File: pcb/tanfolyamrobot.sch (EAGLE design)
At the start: 85 parts, among them IC1 STM32F10XRXT6, IC2 7805, IC4 FT232RL, IC5 LD117AS33TR, M1 DRV8833, Q1 AO4407A, Q2 BSS123, Q3 BSS123, Q4 BSS123, X1 CSTCE08M, X2 PWR, X6 KUSBVX-BS1N

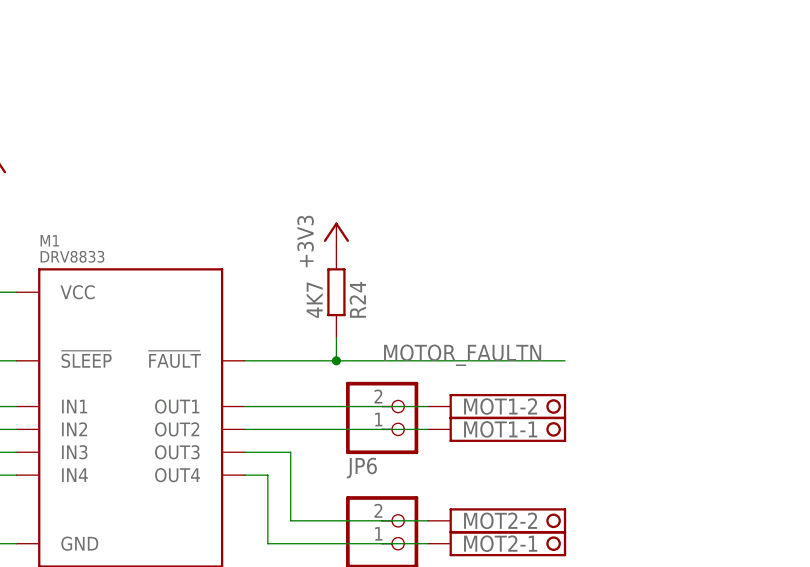
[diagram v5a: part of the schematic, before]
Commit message: removed motor_faultn pullup (#1)
it can be pulled up in stm
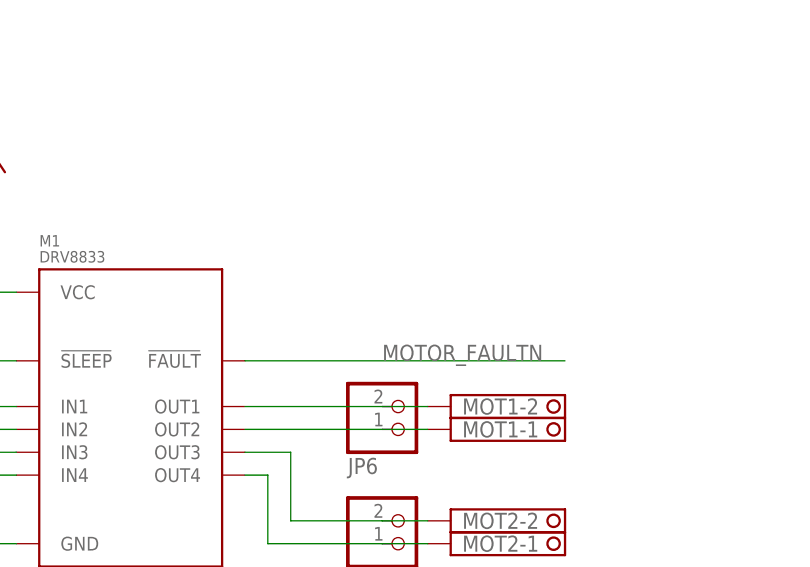
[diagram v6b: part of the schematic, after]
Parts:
- removed R24: 4K7, rcl:R-EU_R0603
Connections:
- net +3V3: no longer R24.1
- net MOTOR_FAULTN: no longer R24.2
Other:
- note added: "Notes: - BUTTON's pin must be pulled up internally - US_TRIG must be operated as open drain output - MOTOR_FAULTN must be pulled up internally"
- note removed: "Notes: - BUTTON's pin must be pulled up internally - US_TRIG must be operated as open drain output"
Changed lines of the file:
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@@
 <part name="GND21" library="supply1" library_urn="urn:adsk.eagle:library:371" deviceset="GND" device=""/>
 <part name="GND22" library="supply1" library_urn="urn:adsk.eagle:library:371" deviceset="GND" device=""/>
-<part name="R24" library="rcl" library_urn="urn:adsk.eagle:library:334" deviceset="R-EU_" device="R0603" package3d_urn="urn:adsk.eagle:package:23555/3" value="4K7"/>
-<part name="+3V10" library="supply1" library_urn="urn:adsk.eagle:library:371" deviceset="+3V3" device=""/>
 <part name="R25" library="rcl" library_urn="urn:adsk.eagle:library:334" deviceset="R-EU_" device="R0603" package3d_urn="urn:adsk.eagle:package:23555/3" value="4K7"/>
 <part name="GND23" library="supply1" library_urn="urn:adsk.eagle:library:371" deviceset="GND" device=""/>
@@
 capacitor to connect FTDI output to
 the RESET and/or BOOT0 circuitry</text>
-<text x="327.66" y="203.2" size="1.778" layer="150">Notes:
+<text x="327.66" y="200.66" size="1.778" layer="150">Notes:
  - BUTTON's pin must be pulled up internally
- - US_TRIG must be operated as open drain output</text>
+ - US_TRIG must be operated as open drain output
+ - MOTOR_FAULTN must be pulled up internally</text>
 <text x="429.26" y="83.82" size="1.778" layer="150">Check if backlight resistor is
 required for the used module</text>
@@
 <instance part="GND22" gate="1" x="368.3" y="248.92" smashed="yes">
 <attribute name="VALUE" x="365.76" y="246.38" size="1.778" layer="96"/>
-</instance>
-<instance part="R24" gate="G$1" x="373.38" y="152.4" smashed="yes" rot="R270">
-<attribute name="NAME" x="374.8786" y="153.67" size="1.778" layer="95" rot="R270"/>
-<attribute name="VALUE" x="370.078" y="153.67" size="1.778" layer="96" rot="R270"/>
-</instance>
-<instance part="+3V10" gate="G$1" x="373.38" y="160.02" smashed="yes">
-<attribute name="VALUE" x="370.84" y="154.94" size="1.778" layer="96" rot="R90"/>
 </instance>
 <instance part="R25" gate="G$1" x="307.34" y="137.16" smashed="yes" rot="R90">
@@
 </segment>
 <segment>
-<pinref part="R24" gate="G$1" pin="1"/>
-<pinref part="+3V10" gate="G$1" pin="+3V3"/>
-</segment>
-<segment>
 <pinref part="R29" gate="G$1" pin="1"/>
 <pinref part="+3V11" gate="G$1" pin="+3V3"/>
@@
 <segment>
 <pinref part="M1" gate="G$1" pin="!FAULT"/>
-<wire x1="363.22" y1="144.78" x2="373.38" y2="144.78" width="0.1524" layer="91"/>
 <label x="378.46" y="144.78" size="1.778" layer="95"/>
-<pinref part="R24" gate="G$1" pin="2"/>
-<wire x1="373.38" y1="144.78" x2="398.78" y2="144.78" width="0.1524" layer="91"/>
-<wire x1="373.38" y1="147.32" x2="373.38" y2="144.78" width="0.1524" layer="91"/>
-<junction x="373.38" y="144.78"/>
-</segment>
-<segment>
+<wire x1="363.22" y1="144.78" x2="398.78" y2="144.78" width="0.1524" layer="91"/>
+</segment>
+<segment>

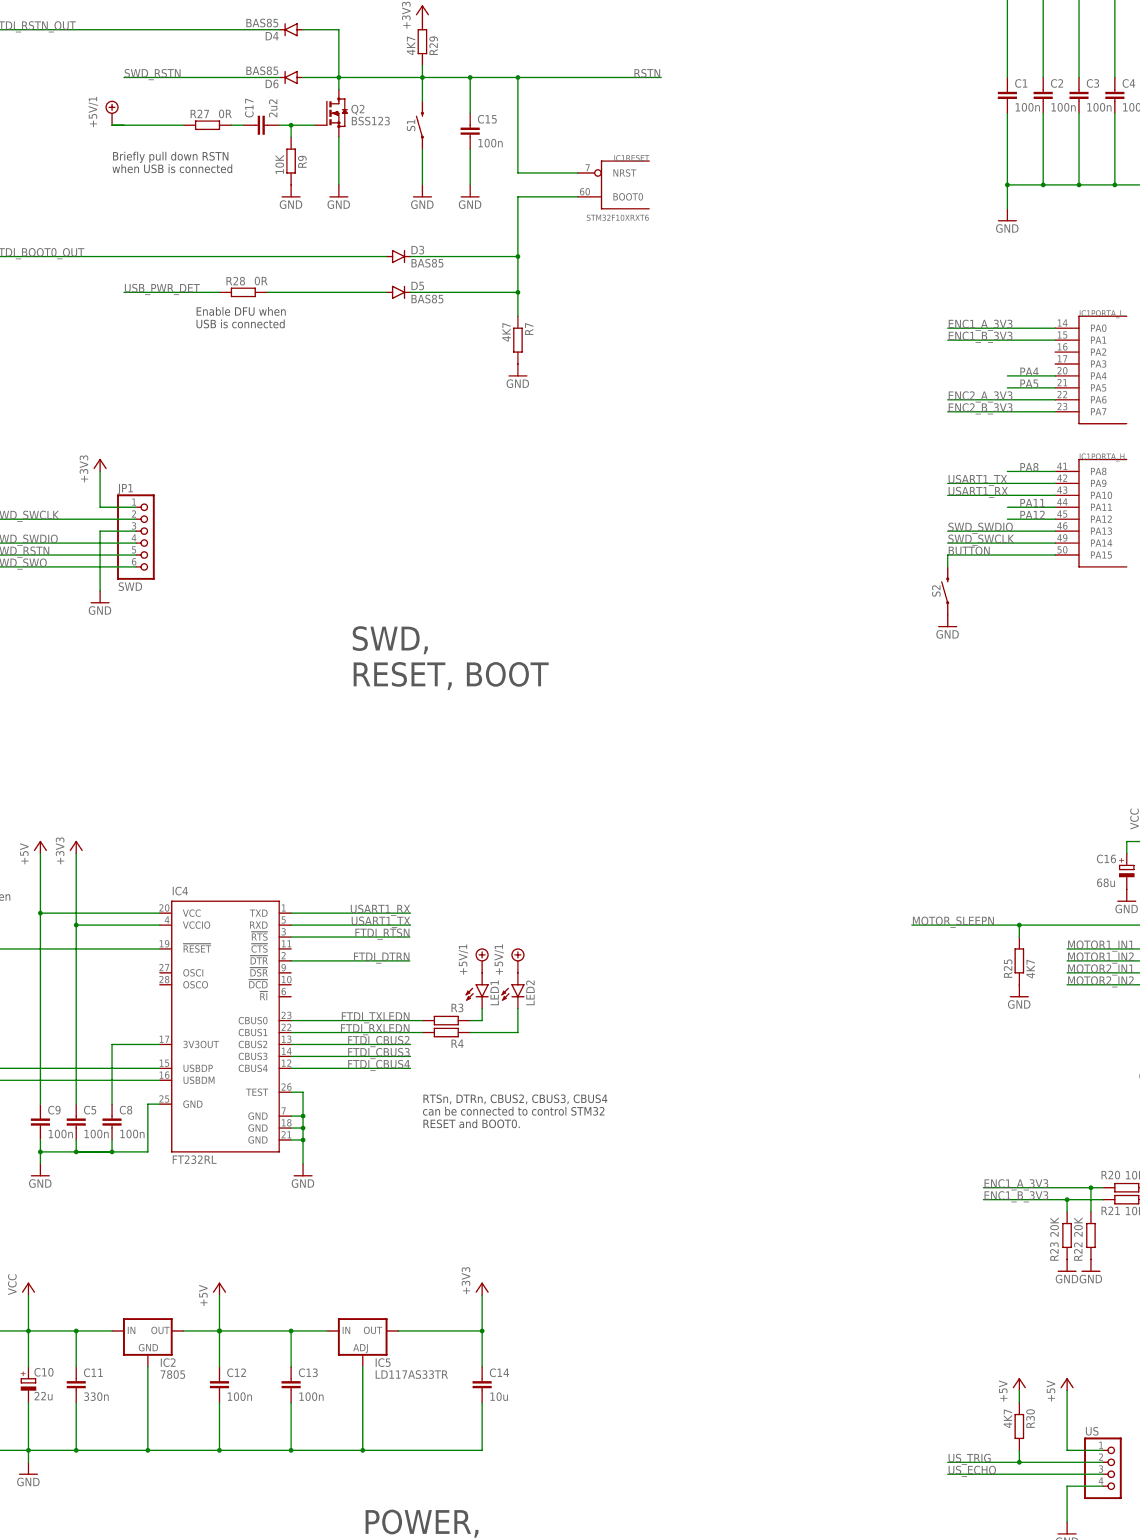
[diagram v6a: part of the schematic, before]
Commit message: added battery voltage measurement (#1)
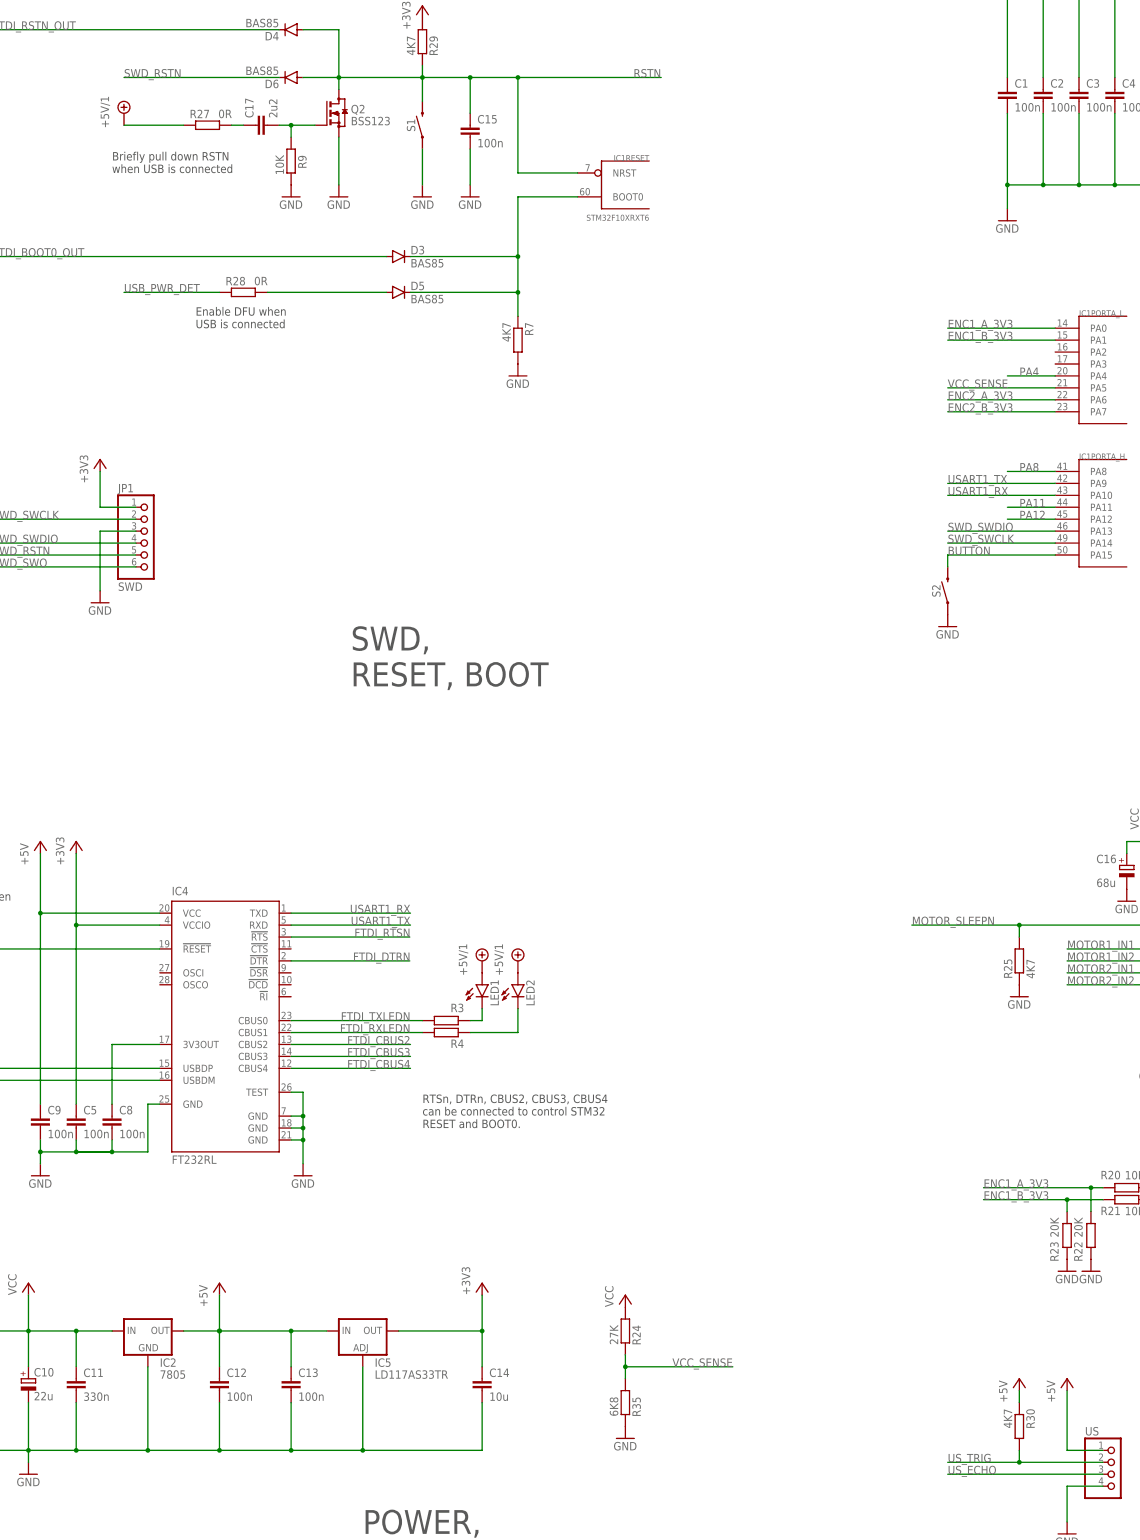
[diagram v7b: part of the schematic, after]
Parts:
- added R24: 27K, rcl:R-EU_R0603
- added R35: 6K8, rcl:R-EU_R0603
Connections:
- removed net PA5: IC1PORTA_L.PA5
- new net VCC_SENSE: IC1PORTA_L.PA5, R24.2, R35.1
- net GND: now also R35.2
- net VCC: now also R24.1
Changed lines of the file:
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@@
 <part name="GND3" library="supply1" library_urn="urn:adsk.eagle:library:371" deviceset="GND" device=""/>
 <part name="GND34" library="supply1" library_urn="urn:adsk.eagle:library:371" deviceset="GND" device=""/>
+<part name="R24" library="rcl" library_urn="urn:adsk.eagle:library:334" deviceset="R-EU_" device="R0603" package3d_urn="urn:adsk.eagle:package:23555/3" value="27K"/>
+<part name="R35" library="rcl" library_urn="urn:adsk.eagle:library:334" deviceset="R-EU_" device="R0603" package3d_urn="urn:adsk.eagle:package:23555/3" value="6K8"/>
+<part name="P+11" library="supply1" library_urn="urn:adsk.eagle:library:371" deviceset="VCC" device=""/>
+<part name="GND36" library="supply1" library_urn="urn:adsk.eagle:library:371" deviceset="GND" device=""/>
 </parts>
 <sheets>
@@
 <attribute name="VALUE" x="197.485" y="133.985" size="1.778" layer="96" rot="R90"/>
 </instance>
-<instance part="SUPPLY4" gate="G$1" x="114.3" y="317.5" smashed="yes">
-<attribute name="VALUE" x="111.125" y="314.325" size="1.778" layer="96" rot="R90"/>
+<instance part="SUPPLY4" gate="G$1" x="116.84" y="317.5" smashed="yes">
+<attribute name="VALUE" x="113.665" y="314.325" size="1.778" layer="96" rot="R90"/>
 </instance>
 <instance part="R30" gate="G$1" x="307.34" y="38.1" smashed="yes" rot="R270">
@@
 <instance part="GND34" gate="1" x="375.92" y="71.12" smashed="yes" rot="MR0">
 <attribute name="VALUE" x="378.46" y="68.58" size="1.778" layer="96" rot="MR0"/>
+</instance>
+<instance part="R24" gate="G$1" x="223.52" y="58.42" smashed="yes" rot="R270">
+<attribute name="NAME" x="225.0186" y="59.69" size="1.778" layer="95" rot="R270"/>
+<attribute name="VALUE" x="220.218" y="59.69" size="1.778" layer="96" rot="R270"/>
+</instance>
+<instance part="R35" gate="G$1" x="223.52" y="43.18" smashed="yes" rot="R270">
+<attribute name="NAME" x="225.0186" y="44.45" size="1.778" layer="95" rot="R270"/>
+<attribute name="VALUE" x="220.218" y="44.45" size="1.778" layer="96" rot="R270"/>
+</instance>
+<instance part="P+11" gate="VCC" x="223.52" y="66.04" smashed="yes">
+<attribute name="VALUE" x="220.98" y="63.5" size="1.778" layer="96" rot="R90"/>
+</instance>
+<instance part="GND36" gate="1" x="223.52" y="35.56" smashed="yes">
+<attribute name="VALUE" x="220.98" y="33.02" size="1.778" layer="96"/>
 </instance>
 </instances>
@@
 <pinref part="GND34" gate="1" pin="GND"/>
 </segment>
+<segment>
+<pinref part="R35" gate="G$1" pin="2"/>
+<pinref part="GND36" gate="1" pin="GND"/>
+</segment>
 </net>
 <net name="+3V3" class="0">
@@
 <wire x1="76.2" y1="58.42" x2="96.52" y2="58.42" width="0.1524" layer="91"/>
 </segment>
+<segment>
+<pinref part="R24" gate="G$1" pin="1"/>
+<pinref part="P+11" gate="VCC" pin="VCC"/>
+</segment>
 </net>
 <net name="N$14" class="0">
@@
 </segment>
 </net>
-<net name="PA5" class="0">
-<segment>
-<pinref part="IC1" gate="PORTA_L" pin="PA5"/>
-<wire x1="314.96" y1="259.08" x2="304.8" y2="259.08" width="0.1524" layer="91"/>
-<label x="307.34" y="259.08" size="1.778" layer="95"/>
-</segment>
-</net>
 <net name="SERVO_5V" class="0">
 <segment>
@@
 <segment>
 <pinref part="SUPPLY4" gate="G$1" pin="+5V/1"/>
-<wire x1="114.3" y1="314.96" x2="116.84" y2="314.96" width="0.1524" layer="91"/>
-<wire x1="129.54" y1="314.96" x2="114.3" y2="314.96" width="0.1524" layer="91"/>
+<wire x1="129.54" y1="314.96" x2="116.84" y2="314.96" width="0.1524" layer="91"/>
 <pinref part="R27" gate="G$1" pin="1"/>
 </segment>
@@
 </segment>
 </net>
+<net name="VCC_SENSE" class="0">
+<segment>
+<pinref part="IC1" gate="PORTA_L" pin="PA5"/>
+<wire x1="314.96" y1="259.08" x2="292.1" y2="259.08" width="0.1524" layer="91"/>
+<label x="292.1" y="259.08" size="1.778" layer="95"/>
+</segment>
+<segment>
+<pinref part="R24" gate="G$1" pin="2"/>
+<pinref part="R35" gate="G$1" pin="1"/>
+<wire x1="223.52" y1="48.26" x2="223.52" y2="50.8" width="0.1524" layer="91"/>
+<wire x1="223.52" y1="50.8" x2="223.52" y2="53.34" width="0.1524" layer="91"/>
+<wire x1="223.52" y1="50.8" x2="246.38" y2="50.8" width="0.1524" layer="91"/>
+<junction x="223.52" y="50.8"/>
+<label x="246.38" y="50.8" size="1.778" layer="95" rot="MR0"/>
+</segment>
+</net>

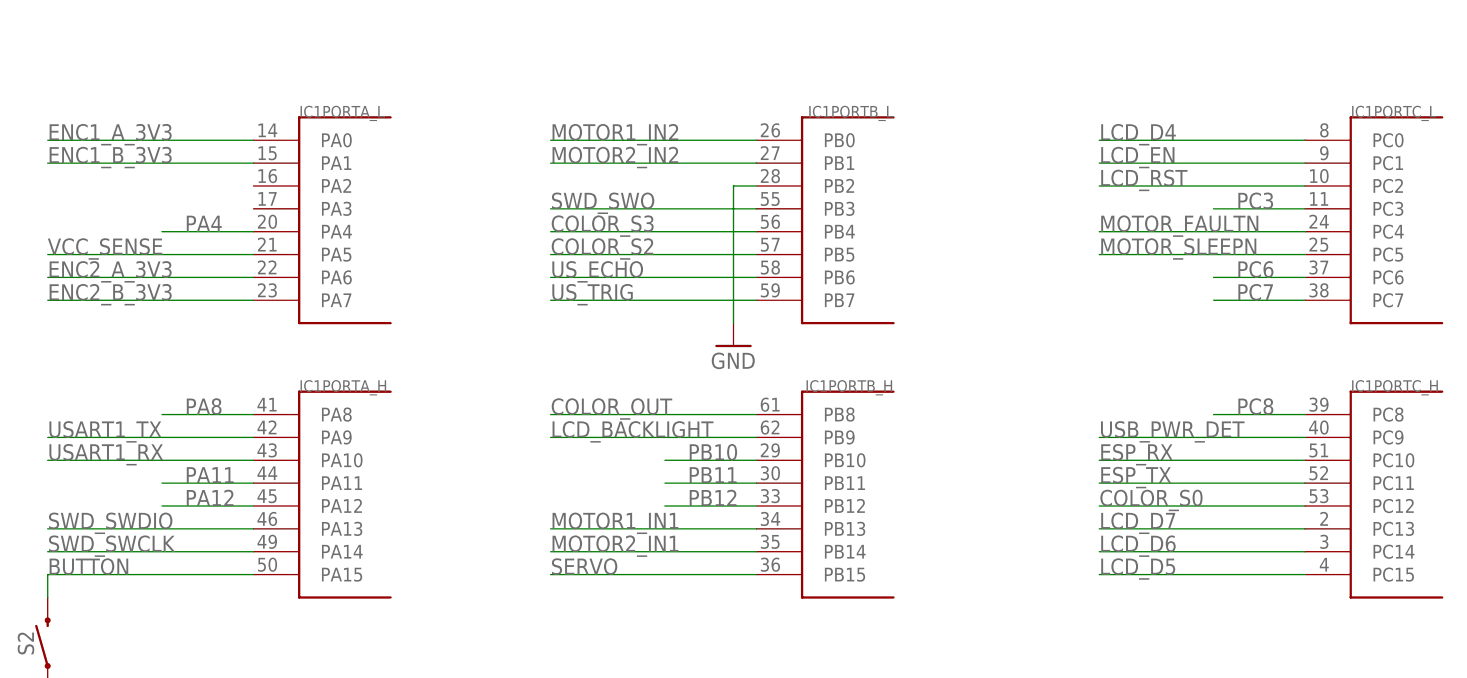
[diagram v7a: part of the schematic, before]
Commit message: fixed unused pins' headers
also had to move some stuff around
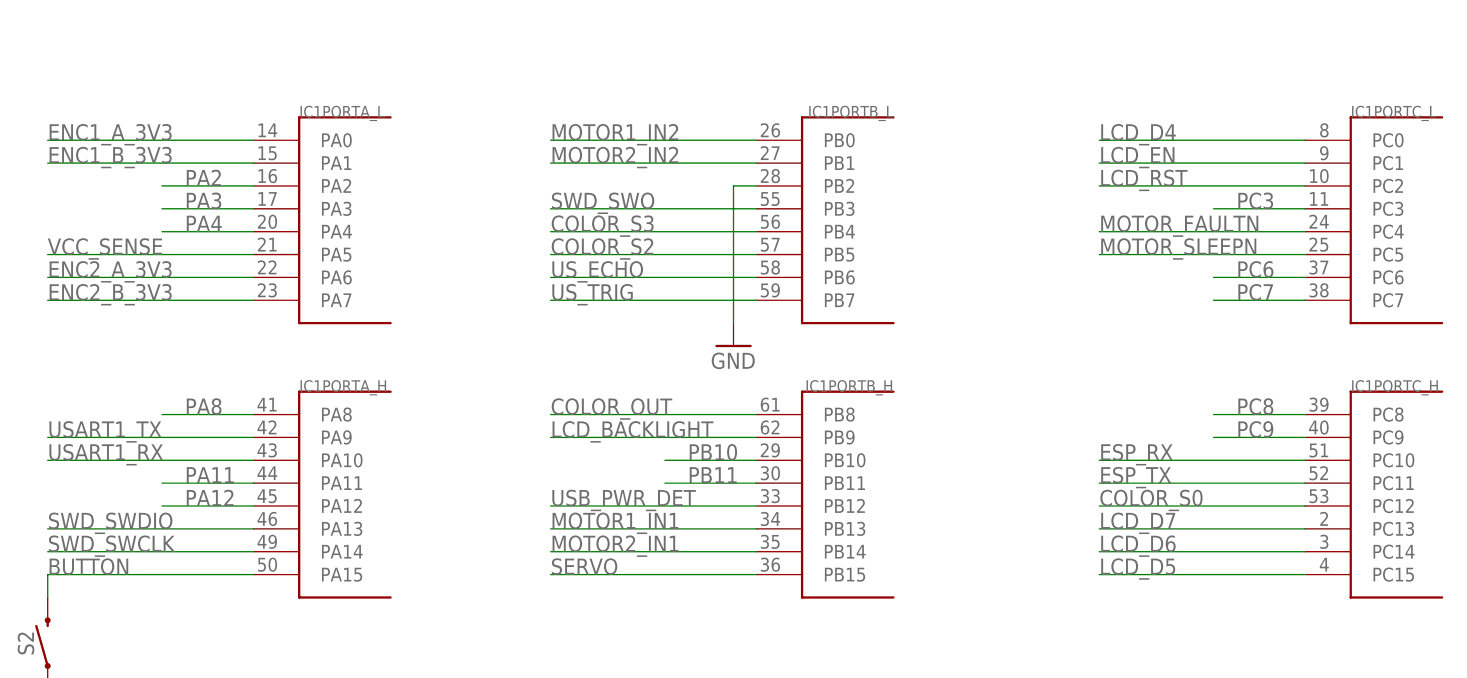
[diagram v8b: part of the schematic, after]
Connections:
- net N$6 renamed LCD_K
- removed net PB12: IC1PORTB_H.PB12
- new net PA2: IC1PORTA_L.PA2
- new net PA3: IC1PORTA_L.PA3
- new net PC9: IC1PORTC_H.PC9
- net USB_PWR_DET: now also IC1PORTB_H.PB12; no longer IC1PORTC_H.PC9
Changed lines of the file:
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@@
 </segment>
 <segment>
-<pinref part="IC1" gate="PORTC_H" pin="PC9"/>
-<wire x1="431.8" y1="238.76" x2="408.94" y2="238.76" width="0.1524" layer="91"/>
-<label x="408.94" y="238.76" size="1.778" layer="95"/>
+<pinref part="IC1" gate="PORTB_H" pin="PB12"/>
+<wire x1="370.84" y1="231.14" x2="347.98" y2="231.14" width="0.1524" layer="91"/>
+<label x="347.98" y="231.14" size="1.778" layer="95"/>
 </segment>
 </net>
@@
 </segment>
 </net>
-<net name="PB12" class="0">
-<segment>
-<pinref part="IC1" gate="PORTB_H" pin="PB12"/>
-<wire x1="370.84" y1="231.14" x2="360.68" y2="231.14" width="0.1524" layer="91"/>
-<label x="363.22" y="231.14" size="1.778" layer="95"/>
-</segment>
-</net>
 <net name="PC8" class="0">
 <segment>
@@
 </segment>
 </net>
-<net name="N$6" class="0">
+<net name="LCD_K" class="0">
 <segment>
 <pinref part="LCD1" gate="G$1" pin="K"/>
@@
 </segment>
 </net>
+<net name="PA2" class="0">
+<segment>
+<pinref part="IC1" gate="PORTA_L" pin="PA2"/>
+<wire x1="314.96" y1="266.7" x2="304.8" y2="266.7" width="0.1524" layer="91"/>
+<label x="307.34" y="266.7" size="1.778" layer="95"/>
+</segment>
+</net>
+<net name="PA3" class="0">
+<segment>
+<pinref part="IC1" gate="PORTA_L" pin="PA3"/>
+<wire x1="314.96" y1="264.16" x2="304.8" y2="264.16" width="0.1524" layer="91"/>
+<label x="307.34" y="264.16" size="1.778" layer="95"/>
+</segment>
+</net>
+<net name="PC9" class="0">
+<segment>
+<pinref part="IC1" gate="PORTC_H" pin="PC9"/>
+<wire x1="431.8" y1="238.76" x2="421.64" y2="238.76" width="0.1524" layer="91"/>
+<label x="424.18" y="238.76" size="1.778" layer="95"/>
+</segment>
+</net>
